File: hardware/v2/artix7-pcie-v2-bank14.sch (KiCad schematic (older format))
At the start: 14 parts, among them J2 Conn_02x20_Odd_Even, U1 XC7A75T-FGG484

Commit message: v2 hardware progress commit - fixed mounting holes and board edge
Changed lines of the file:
@@
 	1    0    0    -1
 $EndComp
-Text HLabel 5300 4800 2    50   Input ~ 0
+Text HLabel 5300 4800 2    50   Output ~ 0
 IO_L16_14_P
 Text HLabel 5300 4900 2    50   Output ~ 0
@@
 Wire Wire Line
 	5150 4000 5300 4000
-Text HLabel 5300 4100 2    50   Output ~ 0
+Text HLabel 5300 4100 2    50   Input ~ 0
 IO_L12_14_N
 Wire Wire Line

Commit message: v2 hardware: j2_34 diff pairs matched, fix 0402 resistor packages, dropped paste from DNP resistors
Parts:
- R8: footprint tom-passives:C_0402_1005Metric -> tom-passives:R_0402_1005Metric
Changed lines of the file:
@@
 F 0 "R8" V 6365 2200 40  0000 C CNN
 F 1 "1k/1%" V 6441 2200 40  0000 C CNN
-F 2 "tom-passives:C_0402_1005Metric" V 6480 2200 30  0001 C CNN
+F 2 "tom-passives:R_0402_1005Metric" V 6480 2200 30  0001 C CNN
 F 3 "" H 6550 2200 30  0001 C CNN
 	1    6550 2200

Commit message: v2 hardware: add Digikey part numbers to schematic and generate bom
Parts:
- C60, C67, C68: Vendor (none) -> 478-12404-1-ND
- C61, C62: Vendor (none) -> 490-5915-1-ND
- C63, C64, C65, C66: Vendor (none) -> 1276-CL05Y474KP5VPNCCT-ND
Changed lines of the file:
@@
 F 2 "tom-passives:C_1206_3216Metric" H 6838 800 30  0001 C CNN
 F 3 "" H 6800 950 60  0001 C CNN
+F 4 "478-12404-1-ND" H 6800 950 50  0001 C CNN "Vendor"
 	1    6800 950
 	1    0    0    -1
@@
 F 2 "tom-passives:C_0402_1005Metric" H 7038 800 30  0001 C CNN
 F 3 "" H 7000 950 60  0001 C CNN
+F 4 "490-5915-1-ND" H 7000 950 50  0001 C CNN "Vendor"
 	1    7000 950
 	1    0    0    -1
@@
 F 2 "tom-passives:C_0402_1005Metric" H 7238 800 30  0001 C CNN
 F 3 "" H 7200 950 60  0001 C CNN
+F 4 "490-5915-1-ND" H 7200 950 50  0001 C CNN "Vendor"
 	1    7200 950
 	1    0    0    -1
@@
 F 2 "tom-passives:C_0402_1005Metric" H 7438 800 30  0001 C CNN
 F 3 "" H 7400 950 60  0001 C CNN
+F 4 "1276-CL05Y474KP5VPNCCT-ND" H 7400 950 50  0001 C CNN "Vendor"
 	1    7400 950
 	1    0    0    -1
@@
 F 2 "tom-passives:C_0402_1005Metric" H 7638 800 30  0001 C CNN
 F 3 "" H 7600 950 60  0001 C CNN
+F 4 "1276-CL05Y474KP5VPNCCT-ND" H 7600 950 50  0001 C CNN "Vendor"
 	1    7600 950
 	1    0    0    -1
@@
 F 2 "tom-passives:C_0402_1005Metric" H 7838 800 30  0001 C CNN
 F 3 "" H 7800 950 60  0001 C CNN
+F 4 "1276-CL05Y474KP5VPNCCT-ND" H 7800 950 50  0001 C CNN "Vendor"
 	1    7800 950
 	1    0    0    -1
@@
 F 2 "tom-passives:C_0402_1005Metric" H 8038 800 30  0001 C CNN
 F 3 "" H 8000 950 60  0001 C CNN
+F 4 "1276-CL05Y474KP5VPNCCT-ND" H 8000 950 50  0001 C CNN "Vendor"
 	1    8000 950
 	1    0    0    -1
@@
 F 2 "tom-passives:C_1206_3216Metric" H 11038 3900 30  0001 C CNN
 F 3 "" H 11000 4050 60  0001 C CNN
+F 4 "478-12404-1-ND" H 11000 4050 50  0001 C CNN "Vendor"
 	1    11000 4050
 	1    0    0    -1
@@
 F 2 "tom-passives:C_1206_3216Metric" H 8338 5350 30  0001 C CNN
 F 3 "" H 8300 5500 60  0001 C CNN
+F 4 "478-12404-1-ND" H 8300 5500 50  0001 C CNN "Vendor"
 	1    8300 5500
 	1    0    0    -1

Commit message: v2 hardware: aug2020 pcb updates
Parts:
- C60, C67, C68: footprint tom-passives:C_1206_3216Metric -> tom-passives:CP_EIA-3216-12_Kemet-S; symbol tom-passives:C -> tom-passives:CP_Small
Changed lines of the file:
@@
 	5300 6500 5150 6500
 $Comp
-L tom-passives:C C?
+L tom-passives:CP_Small C?
 U 1 1 5E981467
 P 6800 950
@@
 F 0 "C60" V 6750 150 40  0000 L CNN
 F 1 "100uF/6.3V/X5R" V 6850 150 40  0000 L CNN
-F 2 "tom-passives:C_1206_3216Metric" H 6838 800 30  0001 C CNN
+F 2 "tom-passives:CP_EIA-3216-12_Kemet-S" H 6838 800 30  0001 C CNN
 F 3 "" H 6800 950 60  0001 C CNN
 F 4 "478-12404-1-ND" H 6800 950 50  0001 C CNN "Vendor"
@@
 Wire Wire Line
 	6800 750  7000 750
-Wire Wire Line
-	6550 1150 6800 1150
-Connection ~ 6800 1150
-Wire Wire Line
-	6800 1150 7000 1150
 $Comp
 L tom-passives:C C?
@@
 VCCO_14
 $Comp
-L tom-passives:C C?
+L tom-passives:CP_Small C?
 U 1 1 5E9A7CA4
 P 11000 4050
@@
 F 0 "C68" H 10900 4450 40  0000 L CNN
 F 1 "100uF/6.3V/X5R" H 10700 4350 40  0000 L CNN
-F 2 "tom-passives:C_1206_3216Metric" H 11038 3900 30  0001 C CNN
+F 2 "tom-passives:CP_EIA-3216-12_Kemet-S" H 11038 3900 30  0001 C CNN
 F 3 "" H 11000 4050 60  0001 C CNN
 F 4 "478-12404-1-ND" H 11000 4050 50  0001 C CNN "Vendor"
@@
 $EndComp
 $Comp
-L tom-passives:C C?
+L tom-passives:CP_Small C?
 U 1 1 5E9B60F9
 P 8300 5500
@@
 F 0 "C67" H 8100 5600 40  0000 L CNN
 F 1 "100uF/6.3V/X5R" H 7650 5450 40  0000 L CNN
-F 2 "tom-passives:C_1206_3216Metric" H 8338 5350 30  0001 C CNN
+F 2 "tom-passives:CP_EIA-3216-12_Kemet-S" H 8338 5350 30  0001 C CNN
 F 3 "" H 8300 5500 60  0001 C CNN
 F 4 "478-12404-1-ND" H 8300 5500 50  0001 C CNN "Vendor"
@@
 	9300 4200 9150 4200
 NoConn ~ 5150 5700
+Wire Wire Line
+	6800 750  6800 850
+Wire Wire Line
+	6550 1150 6800 1150
+Wire Wire Line
+	6800 1050 6800 1150
+Connection ~ 6800 1150
+Wire Wire Line
+	6800 1150 7000 1150
+Wire Wire Line
+	11000 3850 11000 3950
+Wire Wire Line
+	11000 4150 11000 4250
+Wire Wire Line
+	8300 5300 8300 5400
+Wire Wire Line
+	8300 5600 8300 5700
 $EndSCHEMATC

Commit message: v2 hardware: Aug2020/rc2 version - flip tx/rx pairs on s2 - add lcsc part numbers
rc2 errata schematic
- change serial port connector to add +3.3V ? (8-pin)(NO)
- add test points for flash pre-programming
- smaller package on input direction diodes (NO)
- bom dupe errors
- remove all p/s 0R bringup parts
- optimise bom (use 1.5k for led, 10k/4.7k for i2c pullups)
- done led is bright (change to 4.7k)
- improve shield grounding with RC
- check actual values of RGB resistors
- remove caps from clock inputs

rc2 errata pcb
- no gnd marking on serial port connector pins
- change serial port connector to add +3.3V ? (8-pin) (NO)
- no test points for flash pre-programming
- missing caps on xtal? (No but select xtal carefully)
- Cfg sel pins on clock chip?
- No silk on test points
- No +/- pair numbering on silk
- vcc test points for clk pre-programming? (or use bootloader)
- random silk circle under S2
- smaller package on input direction diodes (NO)
- no polarity on 100uF tantalum
- some via in or close to pads
- wrong button package (change from feather to chinese)
- gnd/vcc labels swapped at high end of J2
- clock chip OUT0_SEL_I2CB needs to be tied high after programming
- check teardrops
- power diode footprint marking reverse
- LEDs use cap footprint
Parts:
- C60, C67, C68: LCSC (none) -> C15008
- C61, C62: LCSC (none) -> C23733
- C63, C64, C65, C66: LCSC (none) -> C47339
- J2, TP7, TP8, U1: LCSC (none) -> DNP
- R8: LCSC (none) -> C11702
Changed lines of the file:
@@
 F 2 "tom-passives:R_0402_1005Metric" V 6480 2200 30  0001 C CNN
 F 3 "" H 6550 2200 30  0001 C CNN
+F 4 "C11702" H 6550 2200 50  0001 C CNN "LCSC"
 	1    6550 2200
 	0    1    1    0
@@
 F 2 "artix7-pcie-v2:Socket_Strip_Angled_2x20" H 9500 5000 50  0001 C CNN
 F 3 "~" H 9500 5000 50  0001 C CNN
+F 4 "DNP" H 9500 5000 50  0001 C CNN "LCSC"
 	1    9500 5000
 	1    0    0    1
@@
 F 2 "tom-mechanical:TestPoint_Pad_D1.5mm" H 5950 2300 50  0001 C CNN
 F 3 "~" H 5950 2300 50  0001 C CNN
+F 4 "DNP" H 5750 2300 50  0001 C CNN "LCSC"
 	1    5750 2300
 	0    1    1    0
@@
 F 2 "artix7-pcie-v2:Xilinx_FGG484" H 3150 3800 50  0001 C CNN
 F 3 "" H 3150 3800 50  0000 C CNN
+F 4 "DNP" H 3150 3800 50  0001 C CNN "LCSC"
 	1    3150 3800
 	1    0    0    -1
@@
 F 3 "" H 6800 950 60  0001 C CNN
 F 4 "478-12404-1-ND" H 6800 950 50  0001 C CNN "Vendor"
+F 5 "C15008" H 6800 950 50  0001 C CNN "LCSC"
 	1    6800 950
 	1    0    0    -1
@@
 F 3 "" H 7000 950 60  0001 C CNN
 F 4 "490-5915-1-ND" H 7000 950 50  0001 C CNN "Vendor"
+F 5 "C23733" H 7000 950 50  0001 C CNN "LCSC"
 	1    7000 950
 	1    0    0    -1
@@
 F 3 "" H 7200 950 60  0001 C CNN
 F 4 "490-5915-1-ND" H 7200 950 50  0001 C CNN "Vendor"
+F 5 "C23733" H 7200 950 50  0001 C CNN "LCSC"
 	1    7200 950
 	1    0    0    -1
@@
 F 3 "" H 7400 950 60  0001 C CNN
 F 4 "1276-CL05Y474KP5VPNCCT-ND" H 7400 950 50  0001 C CNN "Vendor"
+F 5 "C47339" H 7400 950 50  0001 C CNN "LCSC"
 	1    7400 950
 	1    0    0    -1
@@
 F 3 "" H 7600 950 60  0001 C CNN
 F 4 "1276-CL05Y474KP5VPNCCT-ND" H 7600 950 50  0001 C CNN "Vendor"
+F 5 "C47339" H 7600 950 50  0001 C CNN "LCSC"
 	1    7600 950
 	1    0    0    -1
@@
 F 3 "" H 7800 950 60  0001 C CNN
 F 4 "1276-CL05Y474KP5VPNCCT-ND" H 7800 950 50  0001 C CNN "Vendor"
+F 5 "C47339" H 7800 950 50  0001 C CNN "LCSC"
 	1    7800 950
 	1    0    0    -1
@@
 F 3 "" H 8000 950 60  0001 C CNN
 F 4 "1276-CL05Y474KP5VPNCCT-ND" H 8000 950 50  0001 C CNN "Vendor"
+F 5 "C47339" H 8000 950 50  0001 C CNN "LCSC"
 	1    8000 950
 	1    0    0    -1
@@
 F 3 "" H 11000 4050 60  0001 C CNN
 F 4 "478-12404-1-ND" H 11000 4050 50  0001 C CNN "Vendor"
+F 5 "C15008" H 11000 4050 50  0001 C CNN "LCSC"
 	1    11000 4050
 	1    0    0    -1
@@
 F 3 "" H 8300 5500 60  0001 C CNN
 F 4 "478-12404-1-ND" H 8300 5500 50  0001 C CNN "Vendor"
+F 5 "C15008" H 8300 5500 50  0001 C CNN "LCSC"
 	1    8300 5500
 	1    0    0    -1
@@
 F 2 "tom-mechanical:TestPoint_Pad_D1.5mm" H 5950 3900 50  0001 C CNN
 F 3 "~" H 5950 3900 50  0001 C CNN
+F 4 "DNP" H 5750 3900 50  0001 C CNN "LCSC"
 	1    5750 3900
 	0    1    1    0

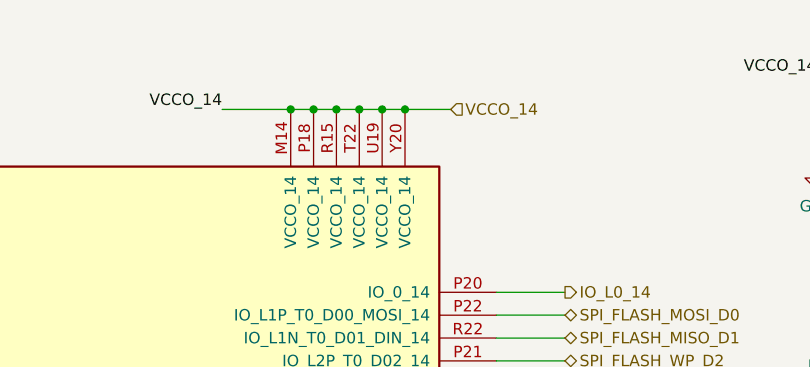
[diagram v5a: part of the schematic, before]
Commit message: JLC power supplies almost routed VCCBRAM to go Need to - check BOM - add power good leds - fix vccbram inc caps - fix 100uF part number - update silk
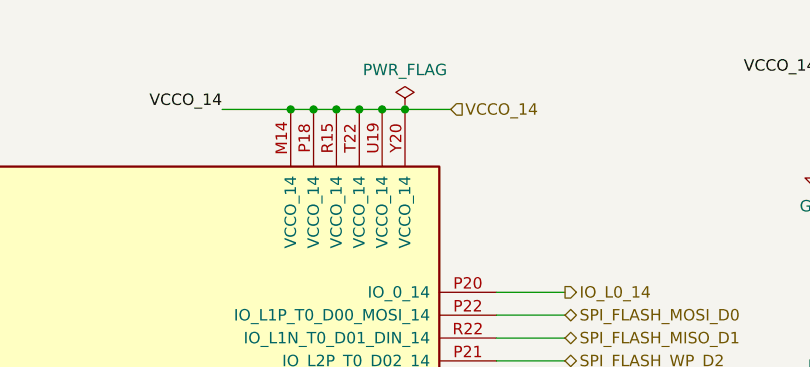
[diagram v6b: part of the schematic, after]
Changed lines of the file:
@@
 Wire Wire Line
 	8300 5600 8300 5700
+$Comp
+L power:PWR_FLAG #FLG0106
+U 1 1 5F933A6D
+P 4750 900
+F 0 "#FLG0106" H 4750 975 50  0001 C CNN
+F 1 "PWR_FLAG" H 4750 1073 50  0000 C CNN
+F 2 "" H 4750 900 50  0001 C CNN
+F 3 "~" H 4750 900 50  0001 C CNN
+	1    4750 900
+	1    0    0    -1
+$EndComp
 $EndSCHEMATC

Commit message: v2 hardware: change 100uF to 3528 for jlcpcb
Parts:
- C60, C67, C68: footprint tom-passives:CP_EIA-3216-12_Kemet-S -> tom-passives:CP_EIA-3528-15_AVX-H
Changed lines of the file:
@@
 F 0 "C60" V 6750 150 40  0000 L CNN
 F 1 "100uF/6.3V/X5R" V 6850 150 40  0000 L CNN
-F 2 "tom-passives:CP_EIA-3216-12_Kemet-S" H 6838 800 30  0001 C CNN
+F 2 "tom-passives:CP_EIA-3528-15_AVX-H" H 6838 800 30  0001 C CNN
 F 3 "" H 6800 950 60  0001 C CNN
 F 4 "478-12404-1-ND" H 6800 950 50  0001 C CNN "Vendor"
@@
 F 0 "C68" H 10900 4450 40  0000 L CNN
 F 1 "100uF/6.3V/X5R" H 10700 4350 40  0000 L CNN
-F 2 "tom-passives:CP_EIA-3216-12_Kemet-S" H 11038 3900 30  0001 C CNN
+F 2 "tom-passives:CP_EIA-3528-15_AVX-H" H 11038 3900 30  0001 C CNN
 F 3 "" H 11000 4050 60  0001 C CNN
 F 4 "478-12404-1-ND" H 11000 4050 50  0001 C CNN "Vendor"
@@
 F 0 "C67" H 8100 5600 40  0000 L CNN
 F 1 "100uF/6.3V/X5R" H 7650 5450 40  0000 L CNN
-F 2 "tom-passives:CP_EIA-3216-12_Kemet-S" H 8338 5350 30  0001 C CNN
+F 2 "tom-passives:CP_EIA-3528-15_AVX-H" H 8338 5350 30  0001 C CNN
 F 3 "" H 8300 5500 60  0001 C CNN
 F 4 "478-12404-1-ND" H 8300 5500 50  0001 C CNN "Vendor"

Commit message: v2 hardware: sep2020 run - fixed issues with parts missing from centroid file
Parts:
- C60, C67, C68: LCSC C15008 -> C16133
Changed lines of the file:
@@
 F 3 "" H 6800 950 60  0001 C CNN
 F 4 "478-12404-1-ND" H 6800 950 50  0001 C CNN "Vendor"
-F 5 "C15008" H 6800 950 50  0001 C CNN "LCSC"
+F 5 "C16133" H 6800 950 50  0001 C CNN "LCSC"
 	1    6800 950
 	1    0    0    -1
@@
 F 3 "" H 11000 4050 60  0001 C CNN
 F 4 "478-12404-1-ND" H 11000 4050 50  0001 C CNN "Vendor"
-F 5 "C15008" H 11000 4050 50  0001 C CNN "LCSC"
+F 5 "C16133" H 11000 4050 50  0001 C CNN "LCSC"
 	1    11000 4050
 	1    0    0    -1
@@
 F 3 "" H 8300 5500 60  0001 C CNN
 F 4 "478-12404-1-ND" H 8300 5500 50  0001 C CNN "Vendor"
-F 5 "C15008" H 8300 5500 50  0001 C CNN "LCSC"
+F 5 "C16133" H 8300 5500 50  0001 C CNN "LCSC"
 	1    8300 5500
 	1    0    0    -1
